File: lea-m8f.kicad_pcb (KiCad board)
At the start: 2 copper layers, 33 parts, among them CON1 USB-MICRO-B, J1 RF_IN, J3 PPS, J4 30.72, P1 CONN_01X08, P2 5V IN, U1 NC7SZ125, U100 B200_GPSDO, U2 LT1962, U3 LEA-M8F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

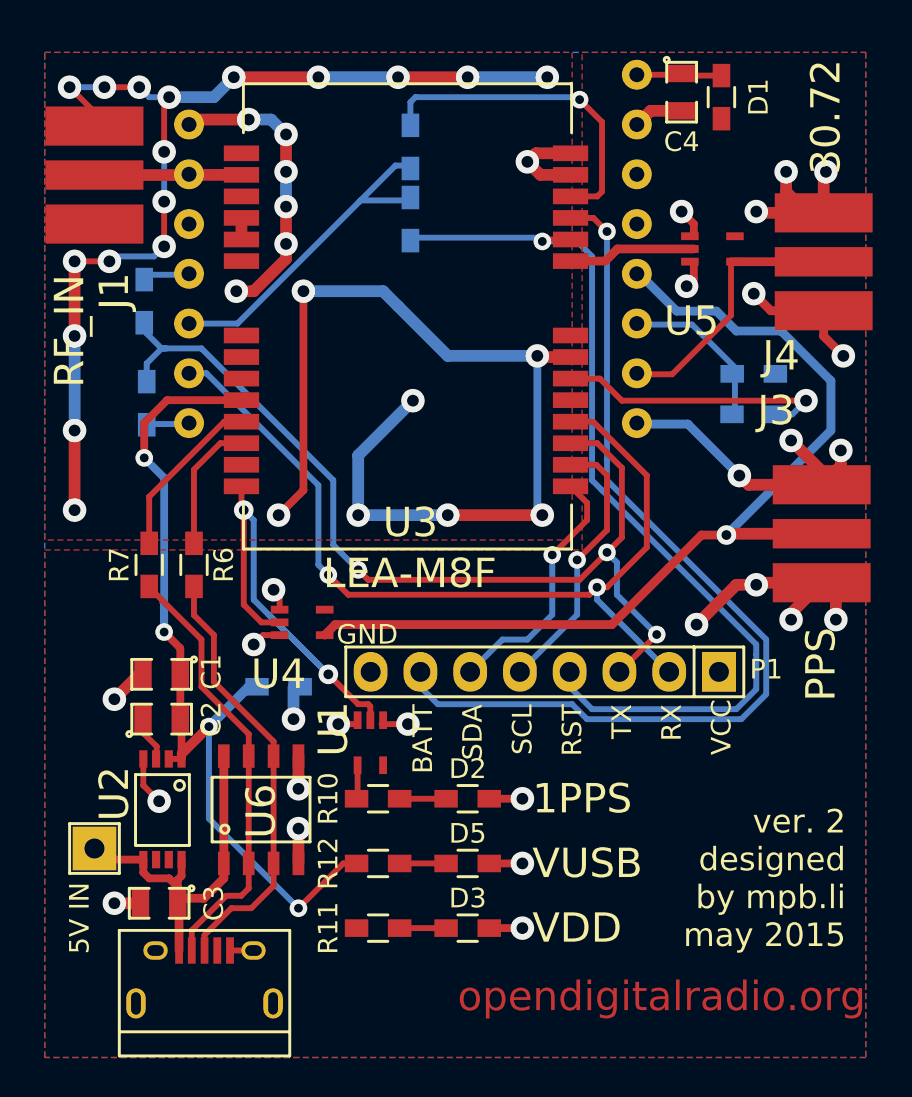
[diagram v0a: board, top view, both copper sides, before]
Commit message: Update footprint for diodes
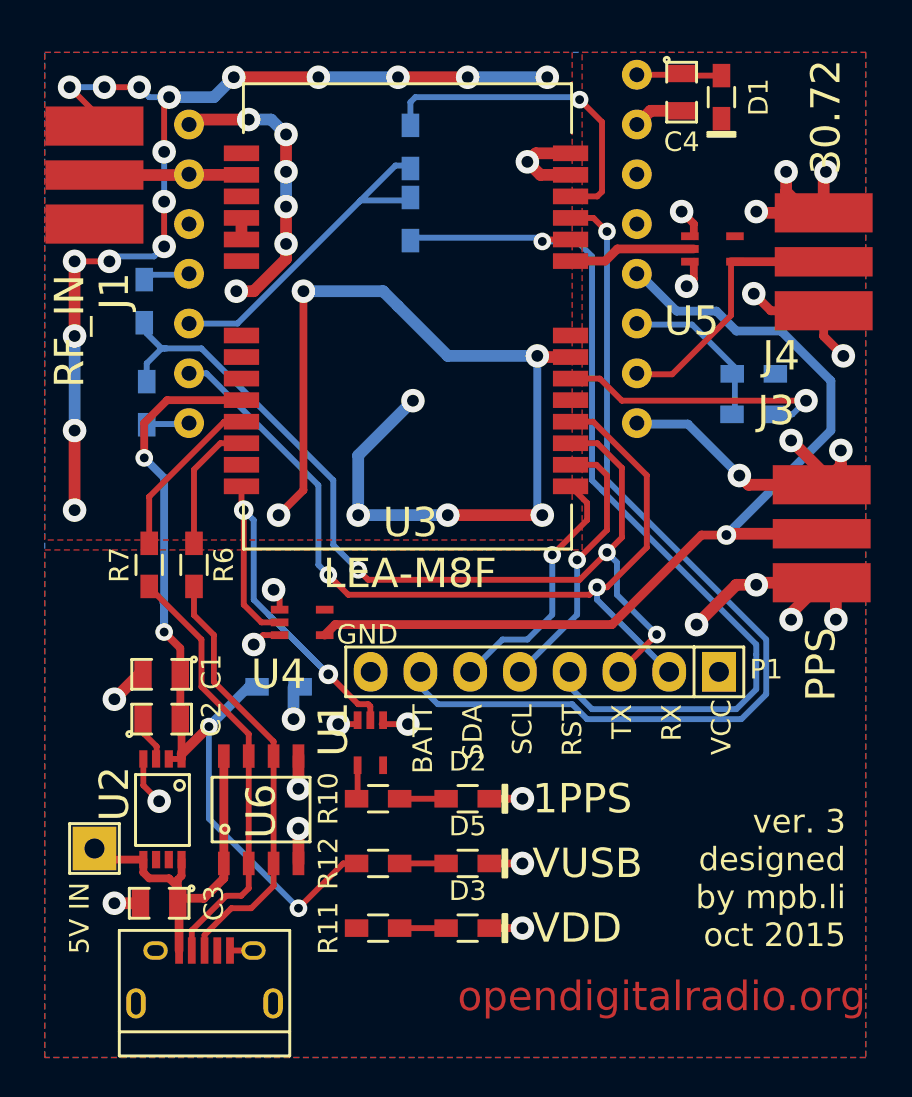
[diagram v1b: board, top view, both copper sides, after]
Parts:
- D1, D2, D3, D4, D5: footprint Resistors_SMD:R_0603_HandSoldering -> lea-m8f:Diode_0603_HandSoldering
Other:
- board text added: "ver. 3 designed by mpb.li oct 2015"
- board text removed: "ver. 2 designed by mpb.li may 2015"
